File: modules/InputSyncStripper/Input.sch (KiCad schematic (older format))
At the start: 33 parts

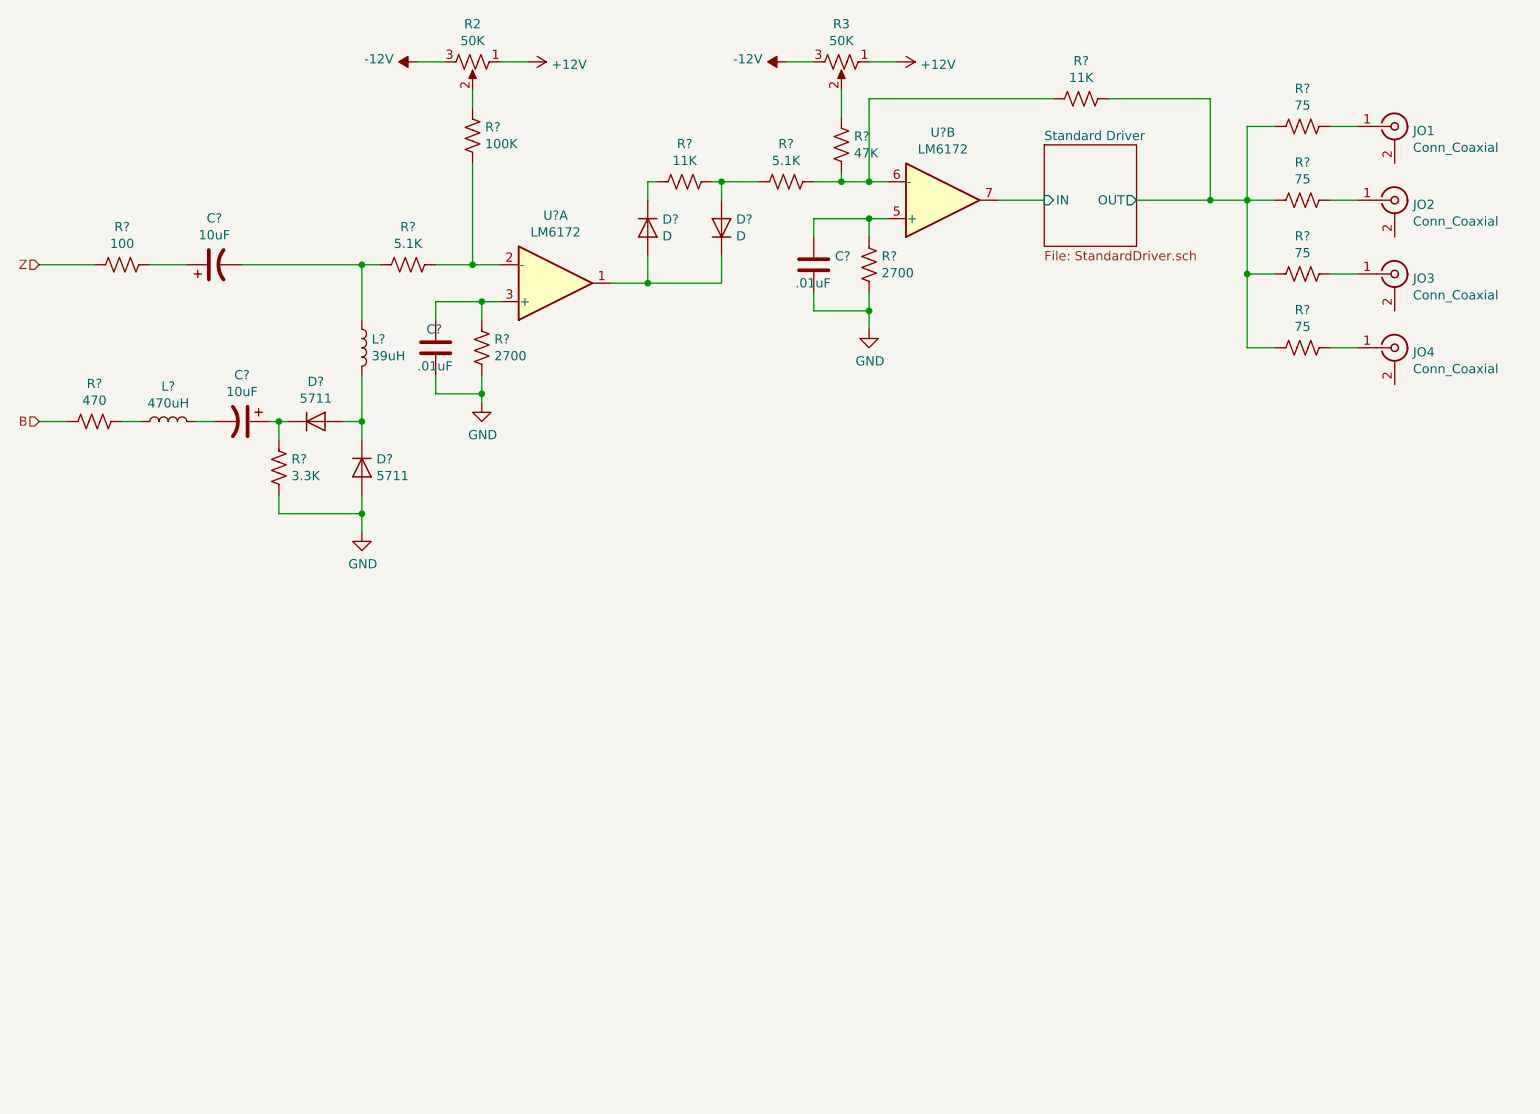
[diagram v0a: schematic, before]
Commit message: fix some ERC issues; assign symbols
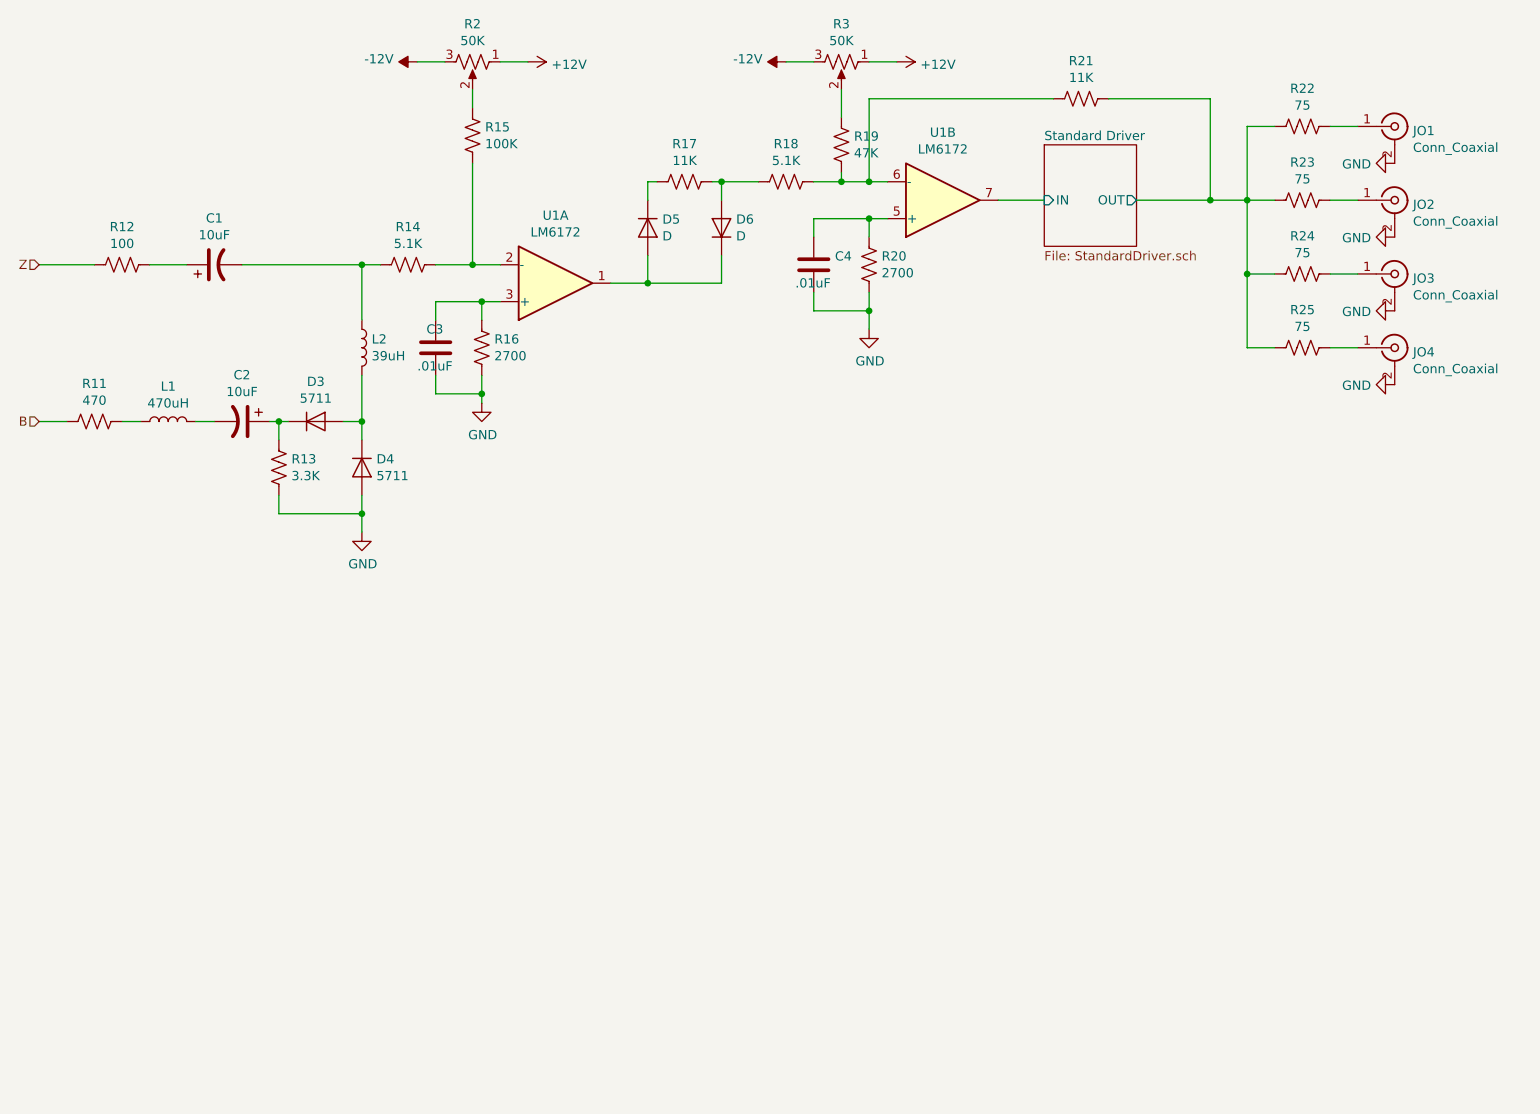
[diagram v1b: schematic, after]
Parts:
- gave numbers to parts that had none: 26
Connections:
- net GND: now also JO1.2 (Ext), JO2.2 (Ext), JO3.2 (Ext), JO4.2 (Ext)
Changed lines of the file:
@@
 EESchema Schematic File Version 4
-LIBS:SIP-cache
+LIBS:InputSyncStripper-cache
 EELAYER 26 0
 EELAYER END
@@
 B
 $Comp
-L Device:R_US R?
+L Device:R_US R11
 U 1 1 5BC7EF5B
 P 1450 4000
-F 0 "R?" V 1245 4000 50  0000 C CNN
+F 0 "R11" V 1245 4000 50  0000 C CNN
 F 1 "470" V 1336 4000 50  0000 C CNN
 F 2 "" V 1490 3990 50  0001 C CNN
@@
 $EndComp
 $Comp
-L Device:L L?
+L Device:L L1
 U 1 1 5BC7F08D
 P 1850 4000
-F 0 "L?" V 2040 4000 50  0000 C CNN
+F 0 "L1" V 2040 4000 50  0000 C CNN
 F 1 "470uH" V 1949 4000 50  0000 C CNN
 F 2 "" H 1850 4000 50  0001 C CNN
@@
 $EndComp
 $Comp
-L Device:R_US R?
+L Device:R_US R12
 U 1 1 5BC7F153
 P 1600 3150
-F 0 "R?" V 1395 3150 50  0000 C CNN
+F 0 "R12" V 1395 3150 50  0000 C CNN
 F 1 "100" V 1486 3150 50  0000 C CNN
 F 2 "" V 1640 3140 50  0001 C CNN
@@
 $EndComp
 $Comp
-L Device:CP1 C?
+L Device:CP1 C1
 U 1 1 5BC7F28A
 P 2100 3150
-F 0 "C?" V 2352 3150 50  0000 C CNN
+F 0 "C1" V 2352 3150 50  0000 C CNN
 F 1 "10uF" V 2261 3150 50  0000 C CNN
 F 2 "" H 2100 3150 50  0001 C CNN
@@
 $EndComp
 $Comp
-L Device:CP1 C?
+L Device:CP1 C2
 U 1 1 5BC7F317
 P 2250 4000
-F 0 "C?" V 1998 4000 50  0000 C CNN
+F 0 "C2" V 1998 4000 50  0000 C CNN
 F 1 "10uF" V 2089 4000 50  0000 C CNN
 F 2 "" H 2250 4000 50  0001 C CNN
@@
 $EndComp
 $Comp
-L Device:L L?
+L Device:L L2
 U 1 1 5BC7F42B
 P 2900 3600
-F 0 "L?" H 2953 3646 50  0000 L CNN
+F 0 "L2" H 2953 3646 50  0000 L CNN
 F 1 "39uH" H 2953 3555 50  0000 L CNN
 F 2 "" H 2900 3600 50  0001 C CNN
@@
 $EndComp
 $Comp
-L Device:D D?
+L Device:D D3
 U 1 1 5BC7F572
 P 2650 4000
-F 0 "D?" H 2650 4216 50  0000 C CNN
+F 0 "D3" H 2650 4216 50  0000 C CNN
 F 1 "5711" H 2650 4125 50  0000 C CNN
 F 2 "" H 2650 4000 50  0001 C CNN
@@
 $EndComp
 $Comp
-L Device:D D?
+L Device:D D4
 U 1 1 5BC7F5C1
 P 2900 4250
-F 0 "D?" V 2854 4329 50  0000 L CNN
+F 0 "D4" V 2854 4329 50  0000 L CNN
 F 1 "5711" V 2945 4329 50  0000 L CNN
 F 2 "" H 2900 4250 50  0001 C CNN
@@
 $EndComp
 $Comp
-L power:GND #PWR?
+L power:GND #PWR05
 U 1 1 5BC7F65D
 P 2900 4600
-F 0 "#PWR?" H 2900 4350 50  0001 C CNN
+F 0 "#PWR05" H 2900 4350 50  0001 C CNN
 F 1 "GND" H 2905 4427 50  0000 C CNN
 F 2 "" H 2900 4600 50  0001 C CNN
@@
 $EndComp
 $Comp
-L Device:R_US R?
+L Device:R_US R13
 U 1 1 5BC7F6D0
 P 2450 4250
-F 0 "R?" H 2518 4296 50  0000 L CNN
+F 0 "R13" H 2518 4296 50  0000 L CNN
 F 1 "3.3K" H 2518 4205 50  0000 L CNN
 F 2 "" V 2490 4240 50  0001 C CNN
@@
 $EndComp
 $Comp
-L Device:R_US R?
+L Device:R_US R14
 U 1 1 5BC7F8DC
 P 3150 3150
-F 0 "R?" V 2945 3150 50  0000 C CNN
+F 0 "R14" V 2945 3150 50  0000 C CNN
 F 1 "5.1K" V 3036 3150 50  0000 C CNN
 F 2 "" V 3190 3140 50  0001 C CNN
@@
 $EndComp
 $Comp
-L Amplifier_Operational:LM6172 U?
+L Amplifier_Operational:LM6172 U1
 U 1 1 5BC7FA02
 P 3950 3250
-F 0 "U?" H 3950 2883 50  0000 C CNN
+F 0 "U1" H 3950 2883 50  0000 C CNN
 F 1 "LM6172" H 3950 2974 50  0000 C CNN
 F 2 "" H 3950 3250 50  0001 C CNN
@@
 $EndComp
 $Comp
-L Device:R_US R?
+L Device:R_US R15
 U 1 1 5BC89253
 P 3500 2450
-F 0 "R?" H 3568 2496 50  0000 L CNN
+F 0 "R15" H 3568 2496 50  0000 L CNN
 F 1 "100K" H 3568 2405 50  0000 L CNN
 F 2 "" V 3540 2440 50  0001 C CNN
@@
 $EndComp
 $Comp
-L Device:D D?
+L Device:D D5
 U 1 1 5BC894F2
 P 4450 2950
-F 0 "D?" V 4404 3029 50  0000 L CNN
+F 0 "D5" V 4404 3029 50  0000 L CNN
 F 1 "D" V 4495 3029 50  0000 L CNN
 F 2 "" H 4450 2950 50  0001 C CNN
@@
 $EndComp
 $Comp
-L Device:D D?
+L Device:D D6
 U 1 1 5BC895B9
 P 4850 2950
-F 0 "D?" V 4896 2871 50  0000 R CNN
+F 0 "D6" V 4896 2871 50  0000 R CNN
 F 1 "D" V 4805 2871 50  0000 R CNN
 F 2 "" H 4850 2950 50  0001 C CNN
@@
 $EndComp
 $Comp
-L Device:R_US R?
+L Device:R_US R17
 U 1 1 5BC896C0
 P 4650 2700
-F 0 "R?" V 4445 2700 50  0000 C CNN
+F 0 "R17" V 4445 2700 50  0000 C CNN
 F 1 "11K" V 4536 2700 50  0000 C CNN
 F 2 "" V 4690 2690 50  0001 C CNN
@@
 $EndComp
 $Comp
-L Device:R_US R?
+L Device:R_US R18
 U 1 1 5BC897EE
 P 5200 2700
-F 0 "R?" V 4995 2700 50  0000 C CNN
+F 0 "R18" V 4995 2700 50  0000 C CNN
 F 1 "5.1K" V 5086 2700 50  0000 C CNN
 F 2 "" V 5240 2690 50  0001 C CNN
@@
 	4450 3250 4250 3250
 $Comp
-L power:GND #PWR?
+L power:GND #PWR07
 U 1 1 5BC8B22A
 P 3550 3900
-F 0 "#PWR?" H 3550 3650 50  0001 C CNN
+F 0 "#PWR07" H 3550 3650 50  0001 C CNN
 F 1 "GND" H 3555 3727 50  0000 C CNN
 F 2 "" H 3550 3900 50  0001 C CNN
@@
 $EndComp
 $Comp
-L Amplifier_Operational:LM6172 U?
+L Amplifier_Operational:LM6172 U1
 U 2 1 5BC8BF9C
 P 6050 2800
-F 0 "U?" H 6050 2433 50  0000 C CNN
+F 0 "U1" H 6050 2433 50  0000 C CNN
 F 1 "LM6172" H 6050 2524 50  0000 C CNN
 F 2 "" H 6050 2800 50  0001 C CNN
@@
 $EndComp
 $Comp
-L Device:R_US R?
+L Device:R_US R19
 U 1 1 5BC8C3D4
 P 5500 2500
-F 0 "R?" H 5568 2546 50  0000 L CNN
+F 0 "R19" H 5568 2546 50  0000 L CNN
 F 1 "47K" H 5568 2455 50  0000 L CNN
 F 2 "" V 5540 2490 50  0001 C CNN
@@
 	5500 2700 5650 2700
 $Comp
-L power:GND #PWR?
+L power:GND #PWR010
 U 1 1 5BC8D2E9
 P 5650 3500
-F 0 "#PWR?" H 5650 3250 50  0001 C CNN
+F 0 "#PWR010" H 5650 3250 50  0001 C CNN
 F 1 "GND" H 5655 3327 50  0000 C CNN
 F 2 "" H 5650 3500 50  0001 C CNN
@@
 $EndSheet
 $Comp
-L Device:R_US R?
+L Device:R_US R21
 U 1 1 5BC8DE58
 P 6800 2250
-F 0 "R?" V 6595 2250 50  0000 C CNN
+F 0 "R21" V 6595 2250 50  0000 C CNN
 F 1 "11K" V 6686 2250 50  0000 C CNN
 F 2 "" V 6840 2240 50  0001 C CNN
@@
 	7500 2800 7100 2800
 $Comp
-L Device:R_US R?
+L Device:R_US R22
 U 1 1 5BC8EBB3
 P 8000 2400
-F 0 "R?" V 7795 2400 50  0000 C CNN
+F 0 "R22" V 7795 2400 50  0000 C CNN
 F 1 "75" V 7886 2400 50  0000 C CNN
 F 2 "" V 8040 2390 50  0001 C CNN
@@
 $EndComp
 $Comp
-L Device:R_US R?
+L Device:R_US R23
 U 1 1 5BC8EC3E
 P 8000 2800
-F 0 "R?" V 7795 2800 50  0000 C CNN
+F 0 "R23" V 7795 2800 50  0000 C CNN
 F 1 "75" V 7886 2800 50  0000 C CNN
 F 2 "" V 8040 2790 50  0001 C CNN
@@
 $EndComp
 $Comp
-L Device:R_US R?
+L Device:R_US R24
 U 1 1 5BC8ECFD
 P 8000 3200
-F 0 "R?" V 7795 3200 50  0000 C CNN
+F 0 "R24" V 7795 3200 50  0000 C CNN
 F 1 "75" V 7886 3200 50  0000 C CNN
 F 2 "" V 8040 3190 50  0001 C CNN
@@
 $EndComp
 $Comp
-L Device:R_US R?
+L Device:R_US R25
 U 1 1 5BC8ED98
 P 8000 3600
-F 0 "R?" V 7795 3600 50  0000 C CNN
+F 0 "R25" V 7795 3600 50  0000 C CNN
 F 1 "75" V 7886 3600 50  0000 C CNN
 F 2 "" V 8040 3590 50  0001 C CNN
@@
 	5650 2700 5750 2700
 $Comp
-L Device:C C?
+L Device:C C3
 U 1 1 5BC9D5ED
 P 3300 3600
-F 0 "C?" H 3250 3700 50  0000 L CNN
+F 0 "C3" H 3250 3700 50  0000 L CNN
 F 1 ".01uF" H 3200 3500 50  0000 L CNN
 F 2 "" H 3338 3450 50  0001 C CNN
@@
 $EndComp
 $Comp
-L Device:R_US R?
+L Device:R_US R16
 U 1 1 5BC9D727
 P 3550 3600
-F 0 "R?" H 3618 3646 50  0000 L CNN
+F 0 "R16" H 3618 3646 50  0000 L CNN
 F 1 "2700" H 3618 3555 50  0000 L CNN
 F 2 "" V 3590 3590 50  0001 C CNN
@@
 $EndComp
 $Comp
-L Device:R_US R?
+L Device:R_US R20
 U 1 1 5BC9D7D6
 P 5650 3150
-F 0 "R?" H 5718 3196 50  0000 L CNN
+F 0 "R20" H 5718 3196 50  0000 L CNN
 F 1 "2700" H 5718 3105 50  0000 L CNN
 F 2 "" V 5690 3140 50  0001 C CNN
@@
 $EndComp
 $Comp
-L Device:C C?
+L Device:C C4
 U 1 1 5BC9D87B
 P 5350 3150
-F 0 "C?" H 5465 3196 50  0000 L CNN
+F 0 "C4" H 5465 3196 50  0000 L CNN
 F 1 ".01uF" H 5250 3050 50  0000 L CNN
 F 2 "" H 5388 3000 50  0001 C CNN
@@
 Connection ~ 5650 3400
 $Comp
-L power:+12V #PWR?
+L power:+12V #PWR08
 U 1 1 5BCA8D87
 P 3800 2050
-F 0 "#PWR?" H 3800 1900 50  0001 C CNN
+F 0 "#PWR08" H 3800 1900 50  0001 C CNN
 F 1 "+12V" V 3815 2178 50  0000 L CNN
 F 2 "" H 3800 2050 50  0001 C CNN
@@
 $EndComp
 $Comp
-L power:+12V #PWR?
+L power:+12V #PWR011
 U 1 1 5BCA8EB1
 P 5800 2050
-F 0 "#PWR?" H 5800 1900 50  0001 C CNN
+F 0 "#PWR011" H 5800 1900 50  0001 C CNN
 F 1 "+12V" V 5815 2178 50  0000 L CNN
 F 2 "" H 5800 2050 50  0001 C CNN
@@
 $EndComp
 $Comp
-L power:-12V #PWR?
+L power:-12V #PWR06
 U 1 1 5BCA8FAB
 P 3200 2050
-F 0 "#PWR?" H 3200 2150 50  0001 C CNN
+F 0 "#PWR06" H 3200 2150 50  0001 C CNN
 F 1 "-12V" V 3215 2178 50  0000 L CNN
 F 2 "" H 3200 2050 50  0001 C CNN
@@
 $EndComp
 $Comp
-L power:-12V #PWR?
+L power:-12V #PWR09
 U 1 1 5BCA9093
 P 5200 2050
-F 0 "#PWR?" H 5200 2150 50  0001 C CNN
+F 0 "#PWR09" H 5200 2150 50  0001 C CNN
 F 1 "-12V" V 5215 2178 50  0000 L CNN
 F 2 "" H 5200 2050 50  0001 C CNN
@@
 Wire Wire Line
 	3650 2050 3800 2050
+$Comp
+L power:GND #PWR0101
+U 1 1 5BCBA7EB
+P 8500 2600
+F 0 "#PWR0101" H 8500 2350 50  0001 C CNN
+F 1 "GND" V 8505 2472 50  0000 R CNN
+F 2 "" H 8500 2600 50  0001 C CNN
+F 3 "" H 8500 2600 50  0001 C CNN
+	1    8500 2600
+	0    1    1    0
+$EndComp
+$Comp
+L power:GND #PWR0102
+U 1 1 5BCBA8FE
+P 8500 3000
+F 0 "#PWR0102" H 8500 2750 50  0001 C CNN
+F 1 "GND" V 8505 2872 50  0000 R CNN
+F 2 "" H 8500 3000 50  0001 C CNN
+F 3 "" H 8500 3000 50  0001 C CNN
+	1    8500 3000
+	0    1    1    0
+$EndComp
+$Comp
+L power:GND #PWR0103
+U 1 1 5BCBAA28
+P 8500 3400
+F 0 "#PWR0103" H 8500 3150 50  0001 C CNN
+F 1 "GND" V 8505 3272 50  0000 R CNN
+F 2 "" H 8500 3400 50  0001 C CNN
+F 3 "" H 8500 3400 50  0001 C CNN
+	1    8500 3400
+	0    1    1    0
+$EndComp
+$Comp
+L power:GND #PWR0104
+U 1 1 5BCBAACE
+P 8500 3800
+F 0 "#PWR0104" H 8500 3550 50  0001 C CNN
+F 1 "GND" V 8505 3672 50  0000 R CNN
+F 2 "" H 8500 3800 50  0001 C CNN
+F 3 "" H 8500 3800 50  0001 C CNN
+	1    8500 3800
+	0    1    1    0
+$EndComp
 $EndSCHEMATC

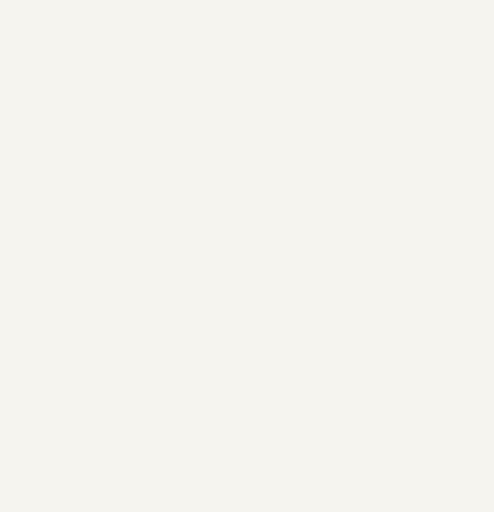
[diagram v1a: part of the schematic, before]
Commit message: added power pins for opamps and tied inputs of unused amp
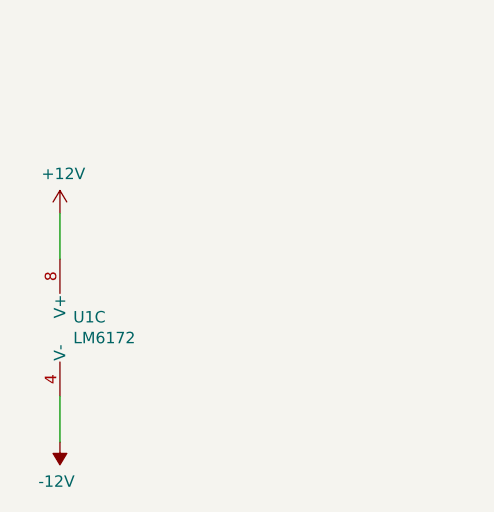
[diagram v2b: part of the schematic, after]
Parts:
- added unit 3 of U1
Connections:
- net +12V: now also U1.8 (V+)
- net -12V: now also U1.4 (V-)
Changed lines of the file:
@@
 	0    1    1    0
 $EndComp
+$Comp
+L Amplifier_Operational:LM6172 U1
+U 3 1 5BCF968F
+P 1300 6950
+F 0 "U1" H 1258 6996 50  0000 L CNN
+F 1 "LM6172" H 1258 6905 50  0000 L CNN
+F 2 "" H 1300 6950 50  0001 C CNN
+F 3 "http://www.ti.com/lit/ds/symlink/lm6172.pdf" H 1300 6950 50  0001 C CNN
+	3    1300 6950
+	1    0    0    -1
+$EndComp
+$Comp
+L power:+12V #PWR0110
+U 1 1 5BCF9838
+P 1200 6450
+F 0 "#PWR0110" H 1200 6300 50  0001 C CNN
+F 1 "+12V" H 1215 6623 50  0000 C CNN
+F 2 "" H 1200 6450 50  0001 C CNN
+F 3 "" H 1200 6450 50  0001 C CNN
+	1    1200 6450
+	1    0    0    -1
+$EndComp
+$Comp
+L power:-12V #PWR0111
+U 1 1 5BCF9943
+P 1200 7450
+F 0 "#PWR0111" H 1200 7550 50  0001 C CNN
+F 1 "-12V" H 1215 7623 50  0000 C CNN
+F 2 "" H 1200 7450 50  0001 C CNN
+F 3 "" H 1200 7450 50  0001 C CNN
+	1    1200 7450
+	-1   0    0    1
+$EndComp
+Wire Wire Line
+	1200 7450 1200 7250
+Wire Wire Line
+	1200 6650 1200 6450
 $EndSCHEMATC

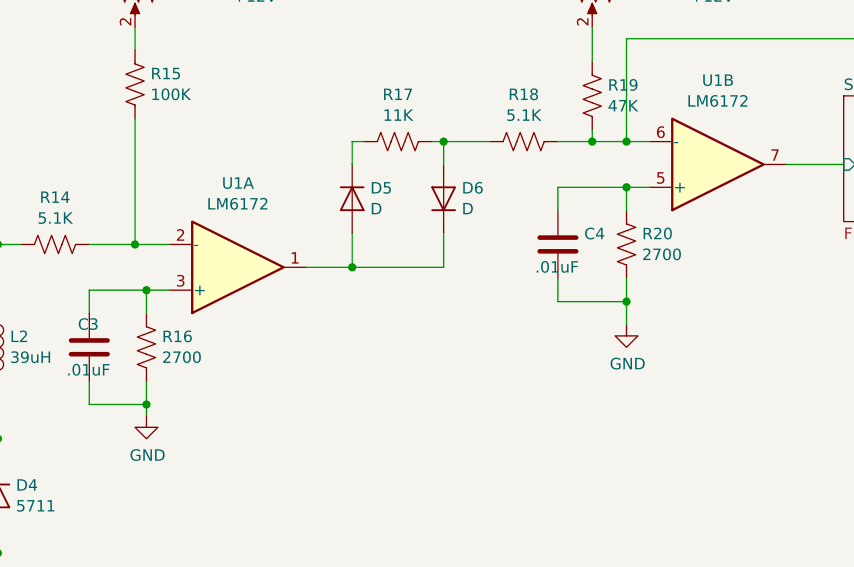
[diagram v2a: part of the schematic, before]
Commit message: Find and fix missing values
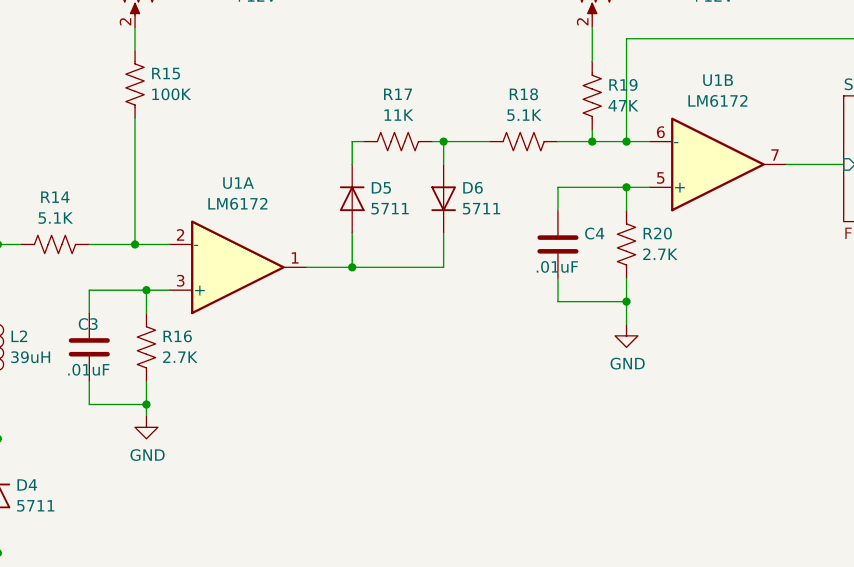
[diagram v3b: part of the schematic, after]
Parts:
- D5, D6: value D -> 5711
- R16, R20: value 2700 -> 2.7K
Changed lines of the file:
@@
 P 4450 2950
 F 0 "D5" V 4404 3029 50  0000 L CNN
-F 1 "D" V 4495 3029 50  0000 L CNN
+F 1 "5711" V 4495 3029 50  0000 L CNN
 F 2 "" H 4450 2950 50  0001 C CNN
 F 3 "~" H 4450 2950 50  0001 C CNN
@@
 P 4850 2950
 F 0 "D6" V 4896 2871 50  0000 R CNN
-F 1 "D" V 4805 2871 50  0000 R CNN
+F 1 "5711" V 4805 2871 50  0000 R CNN
 F 2 "" H 4850 2950 50  0001 C CNN
 F 3 "~" H 4850 2950 50  0001 C CNN
@@
 P 3550 3600
 F 0 "R16" H 3618 3646 50  0000 L CNN
-F 1 "2700" H 3618 3555 50  0000 L CNN
+F 1 "2.7K" H 3618 3555 50  0000 L CNN
 F 2 "" V 3590 3590 50  0001 C CNN
 F 3 "~" H 3550 3600 50  0001 C CNN
@@
 P 5650 3150
 F 0 "R20" H 5718 3196 50  0000 L CNN
-F 1 "2700" H 5718 3105 50  0000 L CNN
+F 1 "2.7K" H 5718 3105 50  0000 L CNN
 F 2 "" V 5690 3140 50  0001 C CNN
 F 3 "~" H 5650 3150 50  0001 C CNN

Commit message: building out footprints/BOM
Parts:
- C1, C2: footprint (none) -> Capacitor_SMD:CP_Elec_5x5.4
- C3, C4: footprint (none) -> Capacitor_SMD:C_0805_2012Metric_Pad1.15x1.40mm_HandSolder
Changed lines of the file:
@@
 F 0 "C1" V 2352 3150 50  0000 C CNN
 F 1 "10uF" V 2261 3150 50  0000 C CNN
-F 2 "" H 2100 3150 50  0001 C CNN
-F 3 "~" H 2100 3150 50  0001 C CNN
+F 2 "Capacitor_SMD:CP_Elec_5x5.4" H 2100 3150 50  0001 C CNN
+F 3 "https://industrial.panasonic.com/cdbs/www-data/pdf/RDE0000/ABA0000C1145.pdf" H 2100 3150 50  0001 C CNN
 	1    2100 3150
 	0    -1   -1   0
@@
 F 0 "C2" V 1998 4000 50  0000 C CNN
 F 1 "10uF" V 2089 4000 50  0000 C CNN
-F 2 "" H 2250 4000 50  0001 C CNN
-F 3 "~" H 2250 4000 50  0001 C CNN
+F 2 "Capacitor_SMD:CP_Elec_5x5.4" H 2250 4000 50  0001 C CNN
+F 3 "https://industrial.panasonic.com/cdbs/www-data/pdf/RDE0000/ABA0000C1145.pdf" H 2250 4000 50  0001 C CNN
 	1    2250 4000
 	0    1    1    0
@@
 F 0 "C3" H 3250 3700 50  0000 L CNN
 F 1 ".01uF" H 3200 3500 50  0000 L CNN
-F 2 "" H 3338 3450 50  0001 C CNN
+F 2 "Capacitor_SMD:C_0805_2012Metric_Pad1.15x1.40mm_HandSolder" H 3338 3450 50  0001 C CNN
 F 3 "~" H 3300 3600 50  0001 C CNN
 	1    3300 3600
@@
 F 0 "C4" H 5465 3196 50  0000 L CNN
 F 1 ".01uF" H 5250 3050 50  0000 L CNN
-F 2 "" H 5388 3000 50  0001 C CNN
+F 2 "Capacitor_SMD:C_0805_2012Metric_Pad1.15x1.40mm_HandSolder" H 5388 3000 50  0001 C CNN
 F 3 "~" H 5350 3150 50  0001 C CNN
 	1    5350 3150
